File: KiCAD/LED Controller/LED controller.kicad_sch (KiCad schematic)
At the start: 37 parts, among them J1 Barrel_Jack_Switch, J2 4x RJ45, J3 Conn_01x24_Female, J4 Conn_01x24_Female, SW1 ELUMOASAQ2C22, SW2 ELUMOASAQ2C22, SW3 ELUMOASAQ2C22, U1 SN75374D, U2 SN75374D, U3 Teensy4.1, U4 SN75374D, U5 SN74LV4053ADR, U6 DAC084S085CIMMX/NOPB, U7 NXB0104PWJ

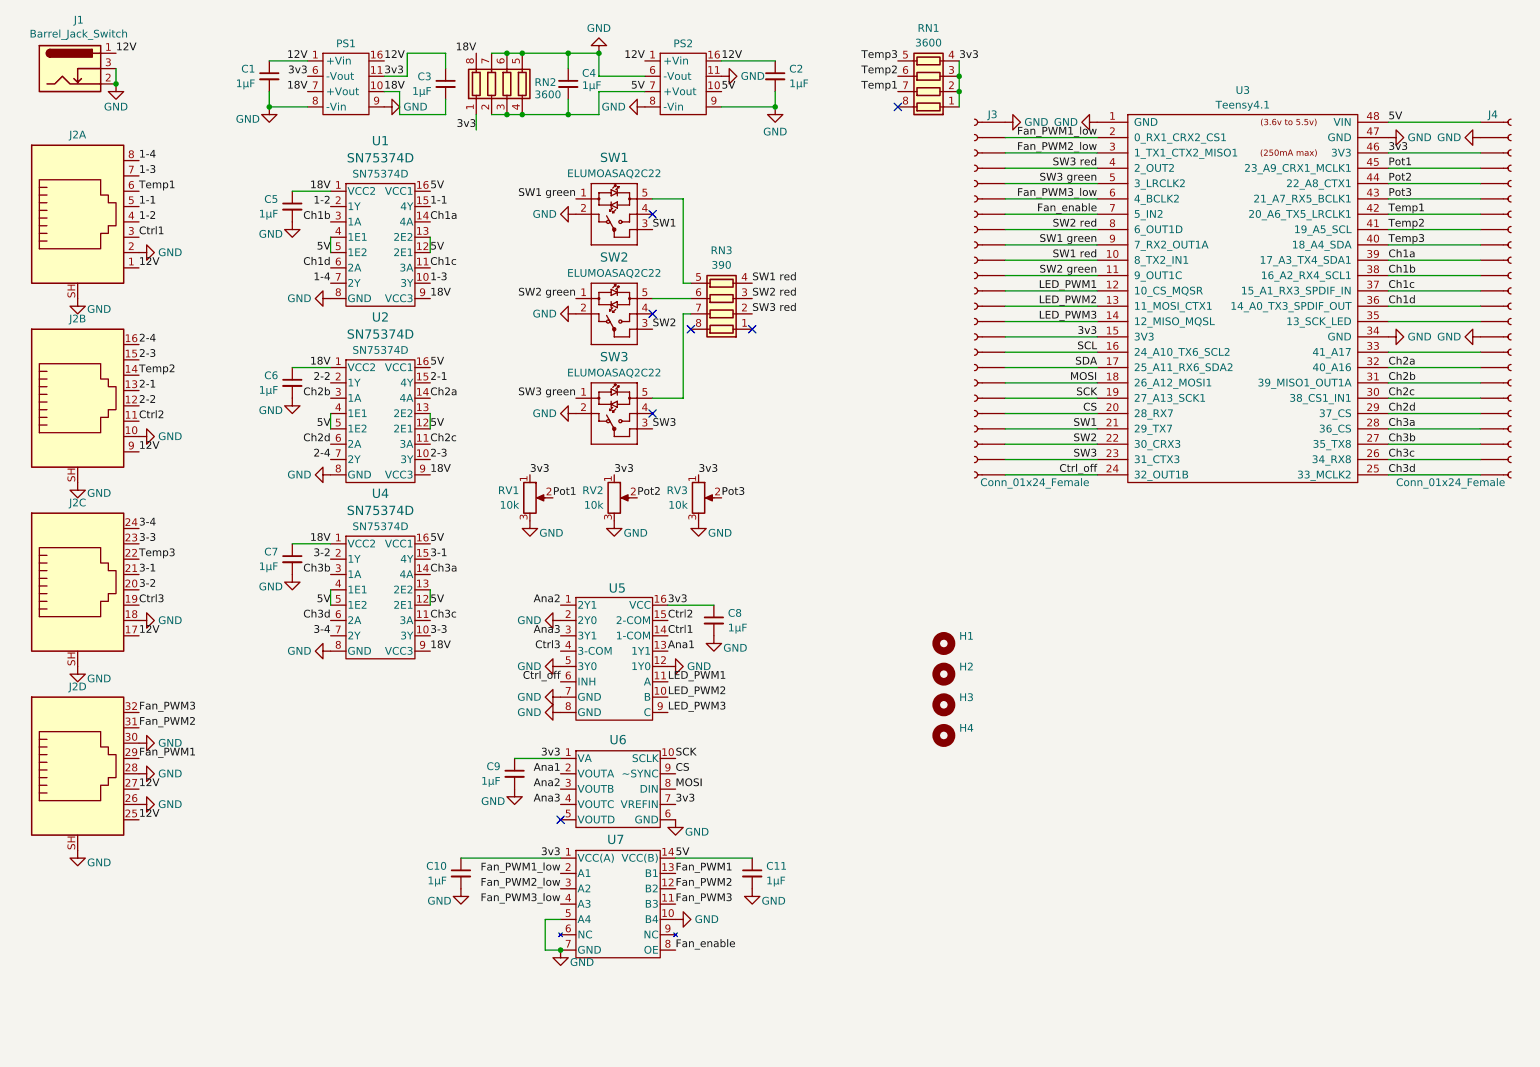
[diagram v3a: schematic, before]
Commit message: Input jack added
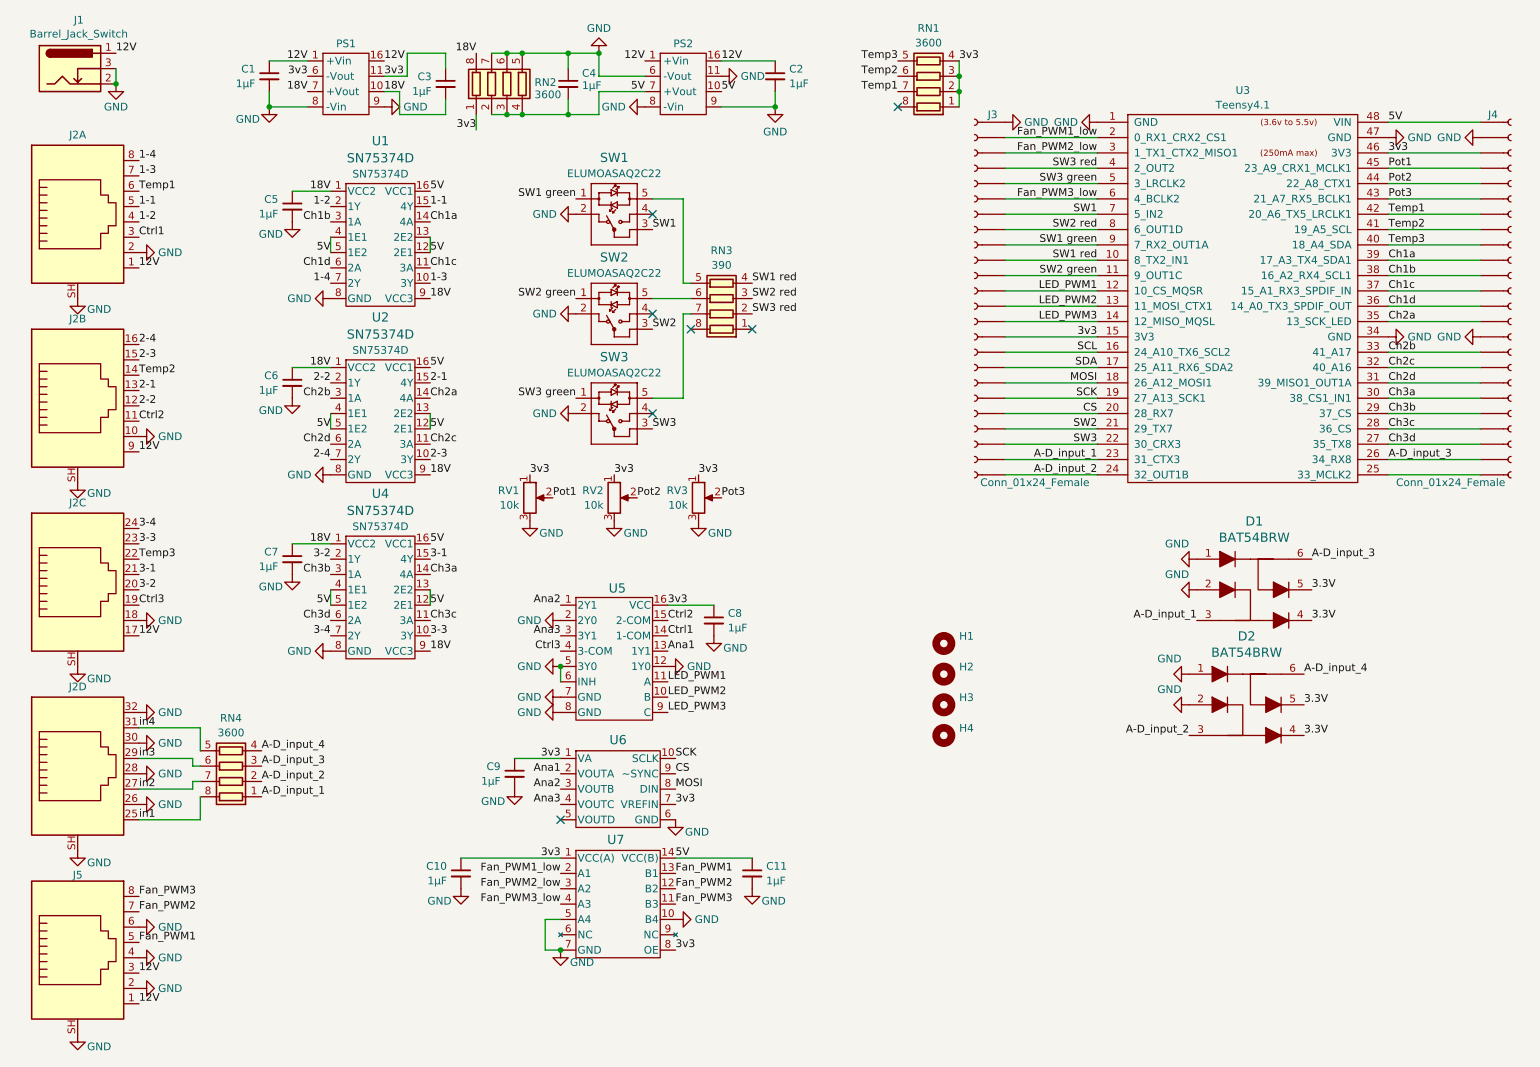
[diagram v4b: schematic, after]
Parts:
- added D1, D2: BAT54BRW, Package_TO_SOT_SMD:SOT-363_SC-70-6, symbol Custom_parts:BAT54BRW
- added J5: 8P8C_Shielded, Custom Footprints:1x RJ45, symbol Connector:8P8C_Shielded
- added RN4: 3600, Resistor_SMD:R_Array_Convex_4x0603, symbol Device:R_Pack04
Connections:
- net 12V: now also J5.1, J5.3; no longer J2.25, J2.27
- net 3v3: now also U7.8 (OE)
- net Ch2a: now also U3.35 (13_SCK_LED); no longer U3.32 (40_A16)
- net Ch2b: now also U3.33 (41_A17); no longer U3.31 (39_MISO1_OUT1A)
- net Ch2c: now also U3.32 (40_A16); no longer U3.30 (38_CS1_IN1)
- net Ch2d: now also U3.31 (39_MISO1_OUT1A); no longer U3.29 (37_CS)
- net Ch3a: now also U3.30 (38_CS1_IN1); no longer U3.28 (36_CS)
- net Ch3b: now also U3.29 (37_CS); no longer U3.27 (35_TX8)
- net Ch3c: now also U3.28 (36_CS); no longer U3.26 (34_RX8)
- net Ch3d: now also U3.27 (35_TX8); no longer U3.25 (33_MCLK2)
- net Fan_PWM1: now also J5.5; no longer J2.29
- net Fan_PWM2: now also J5.7; no longer J2.31
- net Fan_PWM3: now also J5.8; no longer J2.32
- net GND: now also J2.32, U5.6 (INH), D1.1, D1.2, D2.1, D2.2, J5.2, J5.4, J5.6, J5.SH
- net SW1: now also U3.7 (5_IN2); no longer U3.21 (29_TX7)
- net SW2: now also U3.21 (29_TX7); no longer U3.22 (30_CRX3)
- net SW3: now also U3.22 (30_CRX3); no longer U3.23 (31_CTX3)
- removed net Ctrl_off: J3.~, U3.24 (32_OUT1B), U5.6 (INH)
- removed net Fan_enable: J3.~, U3.7 (5_IN2), U7.8 (OE)
- new net: J4.~, U3.25 (33_MCLK2)
- new net 3.3V: D1.4, D1.5, D2.4, D2.5
- new net A-D_input_1: D1.3, J3.~, RN4.1 (R1.1), U3.23 (31_CTX3)
- new net A-D_input_2: D2.3, J3.~, RN4.2 (R2.1), U3.24 (32_OUT1B)
- new net A-D_input_3: D1.6, J4.~, RN4.3 (R3.1), U3.26 (34_RX8)
- new net A-D_input_4: D2.6, RN4.4 (R4.1)
- new net in1: J2.25, RN4.8 (R1.2)
- new net in2: J2.27, RN4.7 (R2.2)
- new net in3: J2.29, RN4.6 (R3.2)
- new net in4: J2.31, RN4.5 (R4.2)

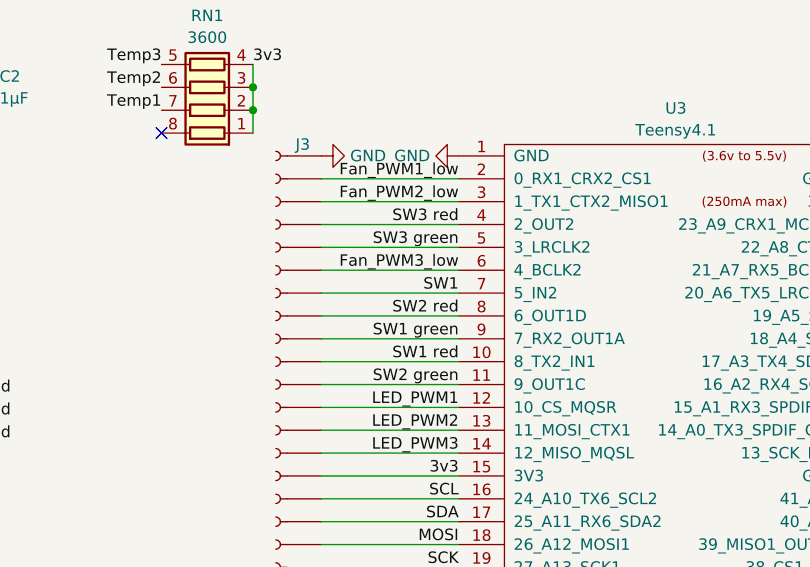
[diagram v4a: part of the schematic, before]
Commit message: Add I/O jack, and re-route
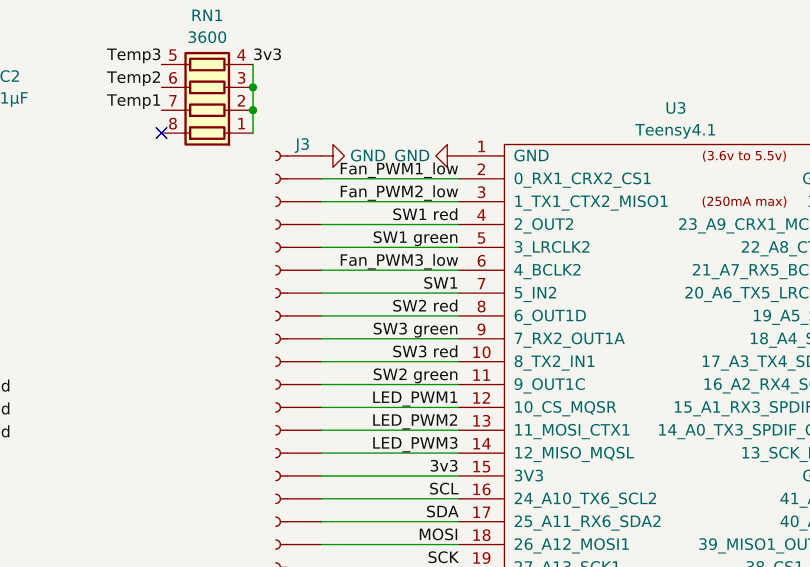
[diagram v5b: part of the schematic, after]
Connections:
- net SW1 green: now also U3.5 (3_LRCLK2); no longer U3.9 (7_RX2_OUT1A)
- net SW1 red: now also U3.4 (2_OUT2); no longer U3.10 (8_TX2_IN1)
- net SW3 green: now also U3.9 (7_RX2_OUT1A); no longer U3.5 (3_LRCLK2)
- net SW3 red: now also U3.10 (8_TX2_IN1); no longer U3.4 (2_OUT2)
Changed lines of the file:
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@@
 	)
 	(label "SW1 red"
-		(at 203.2 63.5 180)
+		(at 203.2 48.26 180)
 		(fields_autoplaced yes)
 		(effects
@@
 	)
 	(label "SW1 green"
-		(at 203.2 60.96 180)
+		(at 203.2 50.8 180)
 		(fields_autoplaced yes)
 		(effects
@@
 	)
 	(label "SW3 red"
-		(at 203.2 48.26 180)
+		(at 203.2 63.5 180)
 		(fields_autoplaced yes)
 		(effects
@@
 	)
 	(label "SW3 green"
-		(at 203.2 50.8 180)
-		(fields_autoplaced yes)
-		(effects
+		(at 203.2 60.96 180)
+		(fields_autoplaced yes)
+		(effects

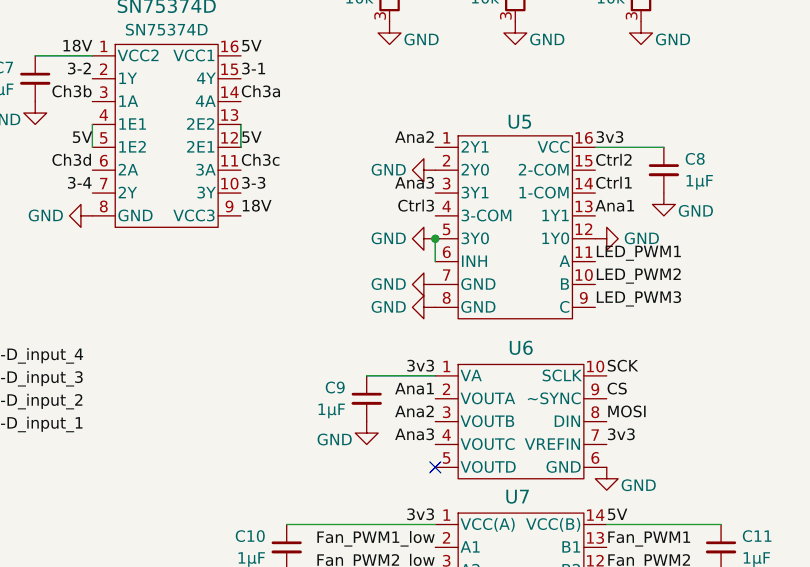
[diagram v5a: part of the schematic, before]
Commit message: more traces added - better grounding
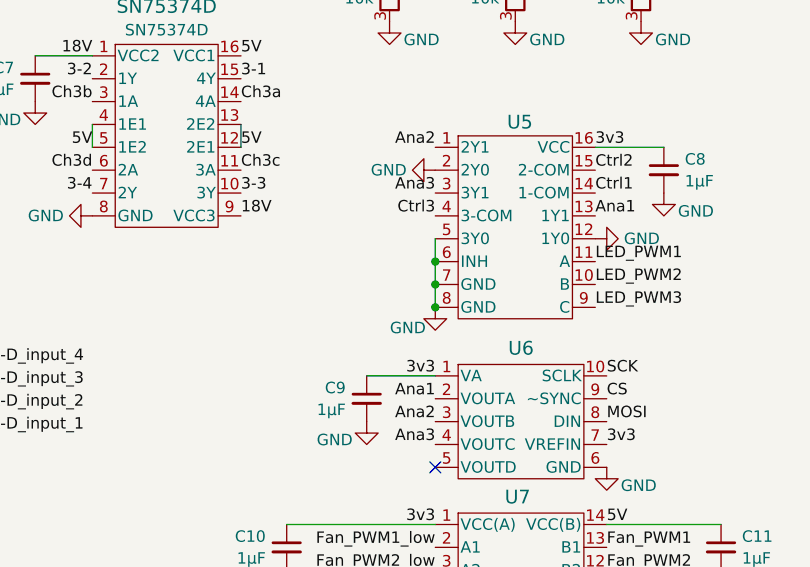
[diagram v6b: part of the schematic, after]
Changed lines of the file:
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@@
 	)
 	(junction
+		(at 114.3 133.35)
+		(diameter 0)
+		(color 0 0 0 0)
+	)
+	(junction
 		(at 40.64 34.29)
 		(diameter 0)
@@
 	)
 	(junction
+		(at 114.3 138.43)
+		(diameter 0)
+		(color 0 0 0 0)
+	)
+	(junction
 		(at 107.95 29.21)
 		(diameter 0)
@@
 	)
 	(junction
-		(at 114.3 130.81)
+		(at 114.3 135.89)
 		(diameter 0)
 		(color 0 0 0 0)
@@
 	(wire
 		(pts
+			(xy 114.3 133.35) (xy 114.3 135.89)
+		)
+		(stroke
+			(width 0)
+			(type default)
+		)
+	)
+	(wire
+		(pts
 			(xy 187.96 63.5) (xy 203.2 63.5)
 		)
@@
 	(wire
 		(pts
+			(xy 114.3 135.89) (xy 114.3 138.43)
+		)
+		(stroke
+			(width 0)
+			(type default)
+		)
+	)
+	(wire
+		(pts
 			(xy 135.89 72.39) (xy 134.62 72.39)
 		)
@@
 	(symbol
 		(lib_id "power:GND")
+		(at 114.3 138.43 0)
+		(unit 1)
+		(exclude_from_sim no)
+		(in_bom yes)
+		(on_board yes)
+		(dnp no)
+		(property "Reference" "#PWR034"
+			(at 114.3 144.78 0)
+			(effects
+				(font
+					(size 1.27 1.27)
+				)
+				(hide yes)
+			)
+		)
+		(property "Value" "GND"
+			(at 111.252 140.716 0)
+			(effects
+				(font
+					(size 1.27 1.27)
+				)
+			)
+		)
+		(property "Footprint" ""
+			(at 114.3 138.43 0)
+			(effects
+				(font
+					(size 1.27 1.27)
+				)
+				(hide yes)
+			)
+		)
+		(property "Datasheet" ""
+			(at 114.3 138.43 0)
+			(effects
+				(font
+					(size 1.27 1.27)
+				)
+				(hide yes)
+			)
+		)
+		(property "Description" "Power symbol creates a global label with name \"GND\" , ground"
+			(at 114.3 138.43 0)
+			(effects
+				(font
+					(size 1.27 1.27)
+				)
+				(hide yes)
+			)
+		)
+		(pin "1"
+		)
+		(instances
+			(project "LED controller"
+				(path "/7e3ae51b-fd56-44ae-a416-05dd2481d5ac"
+					(reference "#PWR034")
+					(unit 1)
+				)
+			)
+		)
+	)
+	(symbol
+		(lib_id "power:GND")
 		(at 76.2 69.85 270)
 		(unit 1)
@@
 	)
 	(symbol
-		(lib_id "power:GND")
-		(at 114.3 135.89 270)
-		(unit 1)
-		(exclude_from_sim no)
-		(in_bom yes)
-		(on_board yes)
-		(dnp no)
-		(fields_autoplaced yes)
-		(property "Reference" "#PWR036"
-			(at 107.95 135.89 0)
-			(effects
-				(font
-					(size 1.27 1.27)
-				)
-				(hide yes)
-			)
-		)
-		(property "Value" "GND"
-			(at 111.1251 135.89 90)
-			(effects
-				(font
-					(size 1.27 1.27)
-				)
-				(justify right)
-			)
-		)
-		(property "Footprint" ""
-			(at 114.3 135.89 0)
-			(effects
-				(font
-					(size 1.27 1.27)
-				)
-				(hide yes)
-			)
-		)
-		(property "Datasheet" ""
-			(at 114.3 135.89 0)
-			(effects
-				(font
-					(size 1.27 1.27)
-				)
-				(hide yes)
-			)
-		)
-		(property "Description" "Power symbol creates a global label with name \"GND\" , ground"
-			(at 114.3 135.89 0)
-			(effects
-				(font
-					(size 1.27 1.27)
-				)
-				(hide yes)
-			)
-		)
-		(pin "1"
-		)
-		(instances
-			(project "LED controller"
-				(path "/7e3ae51b-fd56-44ae-a416-05dd2481d5ac"
-					(reference "#PWR036")
-					(unit 1)
-				)
-			)
-		)
-	)
-	(symbol
 		(lib_id "Custom:SN75374D")
 		(at 71.12 52.07 0)
@@
 	(symbol
 		(lib_id "power:GND")
-		(at 114.3 138.43 270)
-		(unit 1)
-		(exclude_from_sim no)
-		(in_bom yes)
-		(on_board yes)
-		(dnp no)
-		(fields_autoplaced yes)
-		(property "Reference" "#PWR037"
-			(at 107.95 138.43 0)
-			(effects
-				(font
-					(size 1.27 1.27)
-				)
-				(hide yes)
-			)
-		)
-		(property "Value" "GND"
-			(at 111.1251 138.43 90)
-			(effects
-				(font
-					(size 1.27 1.27)
-				)
-				(justify right)
-			)
-		)
-		(property "Footprint" ""
-			(at 114.3 138.43 0)
-			(effects
-				(font
-					(size 1.27 1.27)
-				)
-				(hide yes)
-			)
-		)
-		(property "Datasheet" ""
-			(at 114.3 138.43 0)
-			(effects
-				(font
-					(size 1.27 1.27)
-				)
-				(hide yes)
-			)
-		)
-		(property "Description" "Power symbol creates a global label with name \"GND\" , ground"
-			(at 114.3 138.43 0)
-			(effects
-				(font
-					(size 1.27 1.27)
-				)
-				(hide yes)
-			)
-		)
-		(pin "1"
-		)
-		(instances
-			(project "LED controller"
-				(path "/7e3ae51b-fd56-44ae-a416-05dd2481d5ac"
-					(reference "#PWR037")
-					(unit 1)
-				)
-			)
-		)
-	)
-	(symbol
-		(lib_id "power:GND")
 		(at 139.7 125.73 0)
 		(unit 1)
@@
 					(unit 1)
 				)
-			)
-		)
-	)
-	(symbol
-		(lib_id "power:GND")
-		(at 114.3 130.81 270)
-		(unit 1)
-		(exclude_from_sim no)
-		(in_bom yes)
-		(on_board yes)
-		(dnp no)
-		(fields_autoplaced yes)
-		(property "Reference" "#PWR034"
-			(at 107.95 130.81 0)
-			(effects
-				(font
-					(size 1.27 1.27)
-				)
-				(hide yes)
-			)
-		)
-		(property "Value" "GND"
-			(at 111.1251 130.81 90)
-			(effects
-				(font
-					(size 1.27 1.27)
-				)
-				(justify right)
-			)
-		)
-		(property "Footprint" ""
-			(at 114.3 130.81 0)
-			(effects
-				(font
-					(size 1.27 1.27)
-				)
-				(hide yes)
-			)
-		)
-		(property "Datasheet" ""
-			(at 114.3 130.81 0)
-			(effects
-				(font
-					(size 1.27 1.27)
-				)
-				(hide yes)
-			)
-		)
-		(property "Description" "Power symbol creates a global label with name \"GND\" , ground"
-			(at 114.3 130.81 0)
-			(effects
-				(font
-					(size 1.27 1.27)
-				)
-				(hide yes)
-			)
-		)
-		(pin "1"
-		)
-		(instances
-			(project "LED controller"
-				(path "/7e3ae51b-fd56-44ae-a416-05dd2481d5ac"
-					(reference "#PWR034")
-					(unit 1)
-				)
